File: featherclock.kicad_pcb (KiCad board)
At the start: 4 copper layers, 58.4 x 22.9 mm, 53 parts, among them J1 feather long, J2 feather short, J3 Conn_01x04, J4 USB_C_Receptacle_USB2.0, Q1 MMBT3904, Q2 MMBT3904, SW1 SW_Push, U1 ESP8285, U2 DS3231MZ, U3 74AHCT1G125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

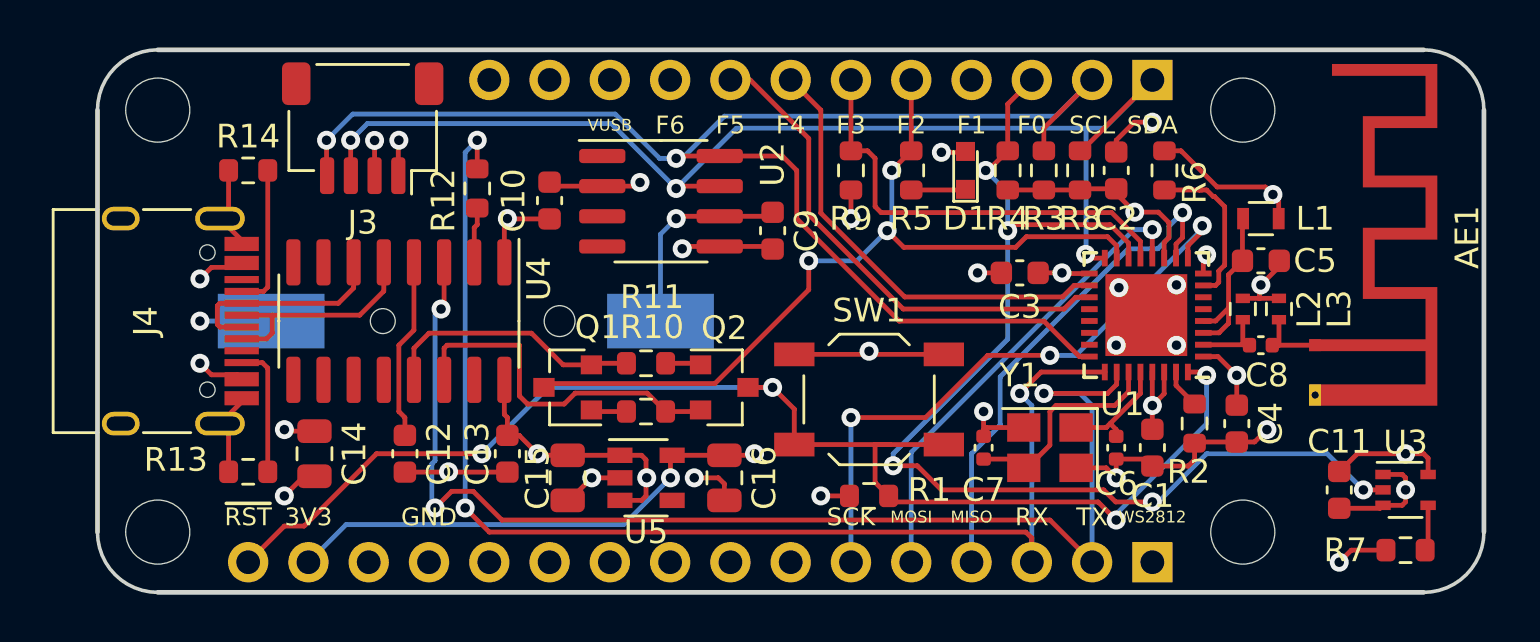
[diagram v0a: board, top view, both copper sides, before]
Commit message: Updated most 0603 packages to 0402
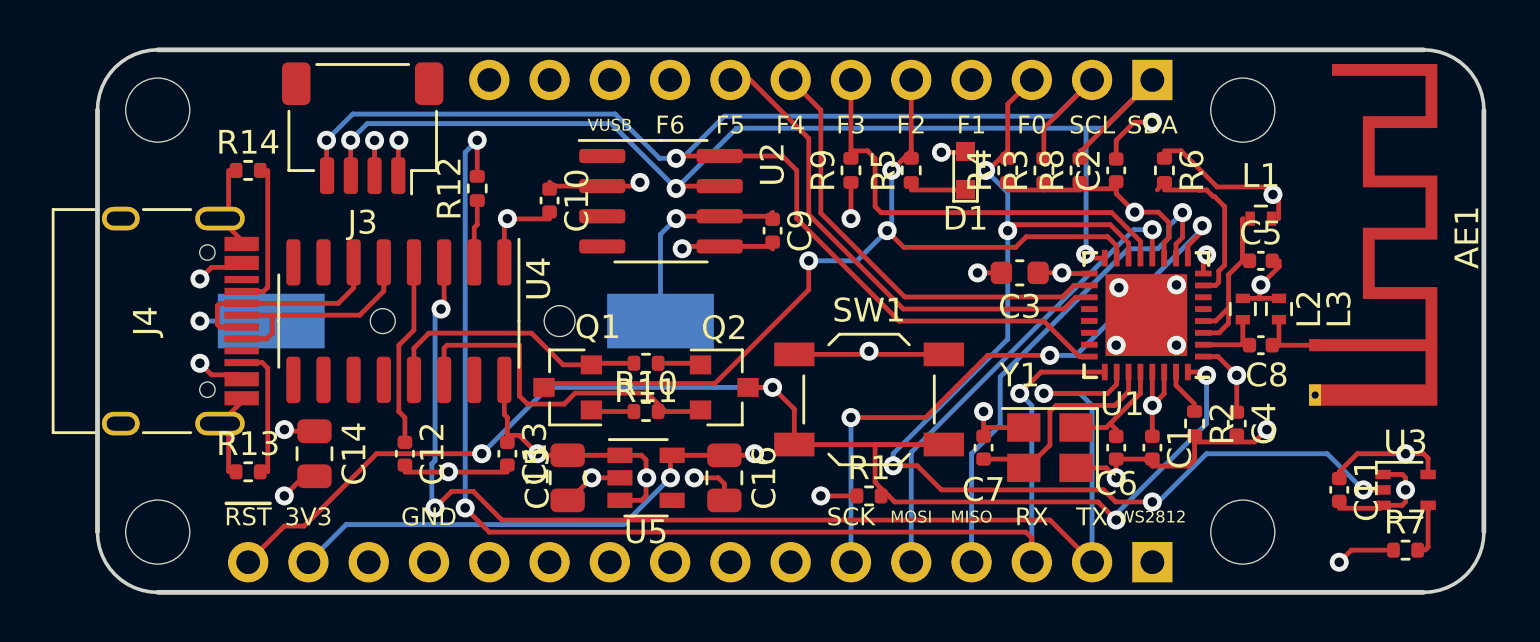
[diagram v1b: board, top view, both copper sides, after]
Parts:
- C1, C10, C11, C12, C13, C2, C4, C5, C9: footprint Capacitor_SMD:C_0603_1608Metric -> Capacitor_SMD:C_0402_1005Metric
- L1: footprint Inductors_SMD:L_0603 -> Inductors_SMD:L_0402
- R1, R10, R11, R12, R13, R14, R2, R3, R4, R5, R6, R7, R8, R9: footprint Resistor_SMD:R_0603_1608Metric -> Resistor_SMD:R_0402_1005Metric

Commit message: Cleaned up for new 0402 parts, and rearranged parts now that we have so much space.
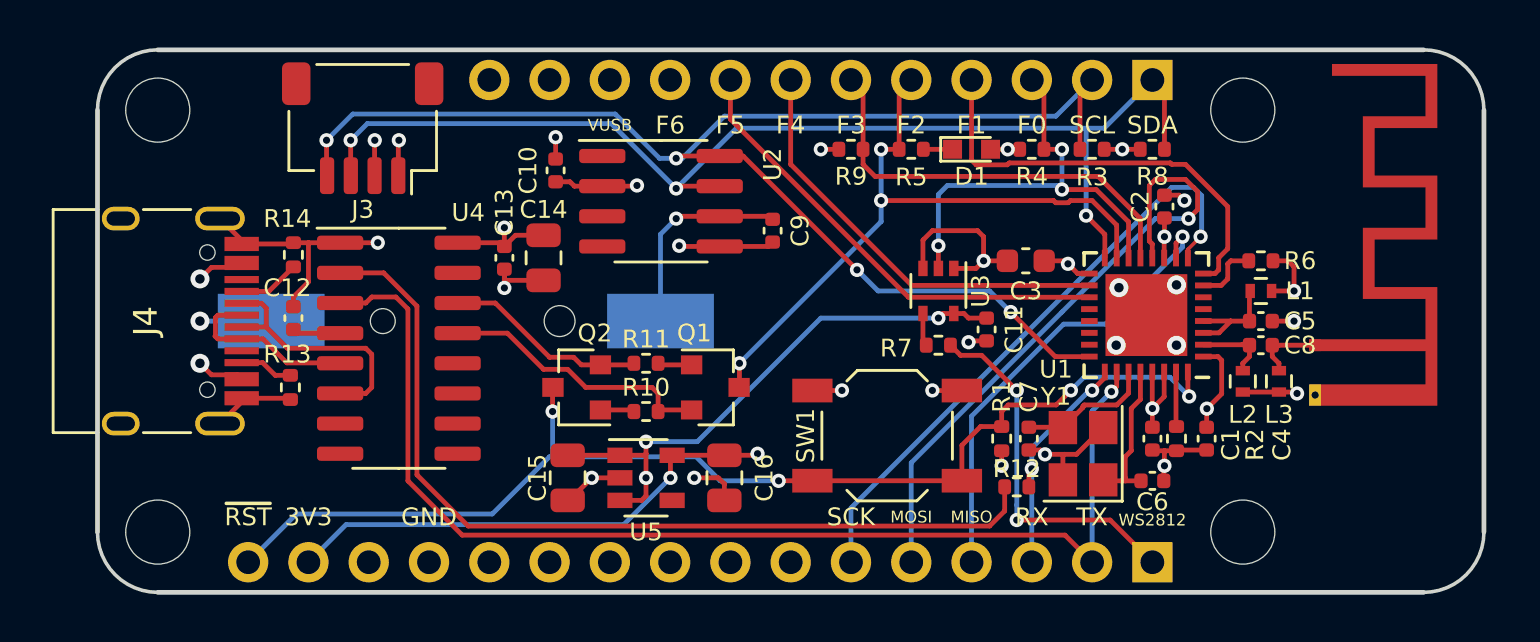
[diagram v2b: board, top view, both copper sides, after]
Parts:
- moved R12 26.0 mm to (64.1, 43.8), turned to 0 degrees
- moved R7 21.5 mm to (60.8, 37.8), turned to 180 degrees
- moved U3 21.4 mm to (60.8, 35.6), turned to 270 degrees
- moved C11 16.3 mm to (62.9, 37.2)
- moved C14 12.7 mm to (44.2, 34.2)
- moved C13 8.26 mm to (42.5, 34.2)
- moved C12 7.40 mm to (33.7, 36.7), turned to 90 degrees
- moved Q1 6.22 mm to (51.4, 39.6), turned to 0 degrees
- moved Q2 6.22 mm to (45.6, 39.6), turned to 180 degrees
- moved R1 6.09 mm to (63.5, 41.8), turned to 90 degrees
- moved R6 5.57 mm to (74.4, 34.3), turned to 180 degrees
- moved R14 4.03 mm to (33.7, 34.0), turned to 270 degrees
- moved R13 3.98 mm to (33.5, 39.6), turned to 90 degrees
- moved R8 3.17 mm to (69.8, 29.6), turned to 0 degrees
- moved L1 3.05 mm to (74.4, 35.6)
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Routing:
- net /RX: track 53.6 -> 10.2 mm, vias 3 -> 2
- net Net-(R12-Pad1): track 2.34 -> 37.9 mm
- net /GPIO2: track 48.4 -> 19.0 mm, vias 5 -> 3
- net VCC: track 21.6 -> 32.2 mm
- net +3V3: track 53.6 -> 44.6 mm, vias 11 -> 12
- net GND: track 64.7 -> 56.8 mm, vias 21 -> 22
- net /RESET: track 56.8 -> 49.3 mm
- net /GPIO0: track 35.5 -> 28.2 mm
- net /GPIO13-MOSI: track 19.9 -> 26.9 mm
- net /RTS: track 15.0 -> 8.54 mm
- net Net-(C12-Pad1): track 7.66 -> 2.03 mm
- net /WS2812: track 10.7 -> 15.5 mm, vias 1 -> 2
- net Net-(R6-Pad2): track 7.02 -> 2.72 mm
- net Net-(C7-Pad1): track 9.25 -> 5.73 mm
- net Net-(J4-PadA5): track 6.09 -> 2.61 mm
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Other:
- net class Default: clearance 0.2 -> 0.1524; trace_width 0.25 -> 0.1524; via_dia 0.8 -> 0.6; via_drill 0.4 -> 0.3
- rule trace_clearance: 0.2 -> 0.1524
- rule via_min_drill: 0.3 -> 0.2

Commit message: Added tooling holes and fiducials. Extended board outline under USB connector. Ran DRC, looks good - can probably order these now.
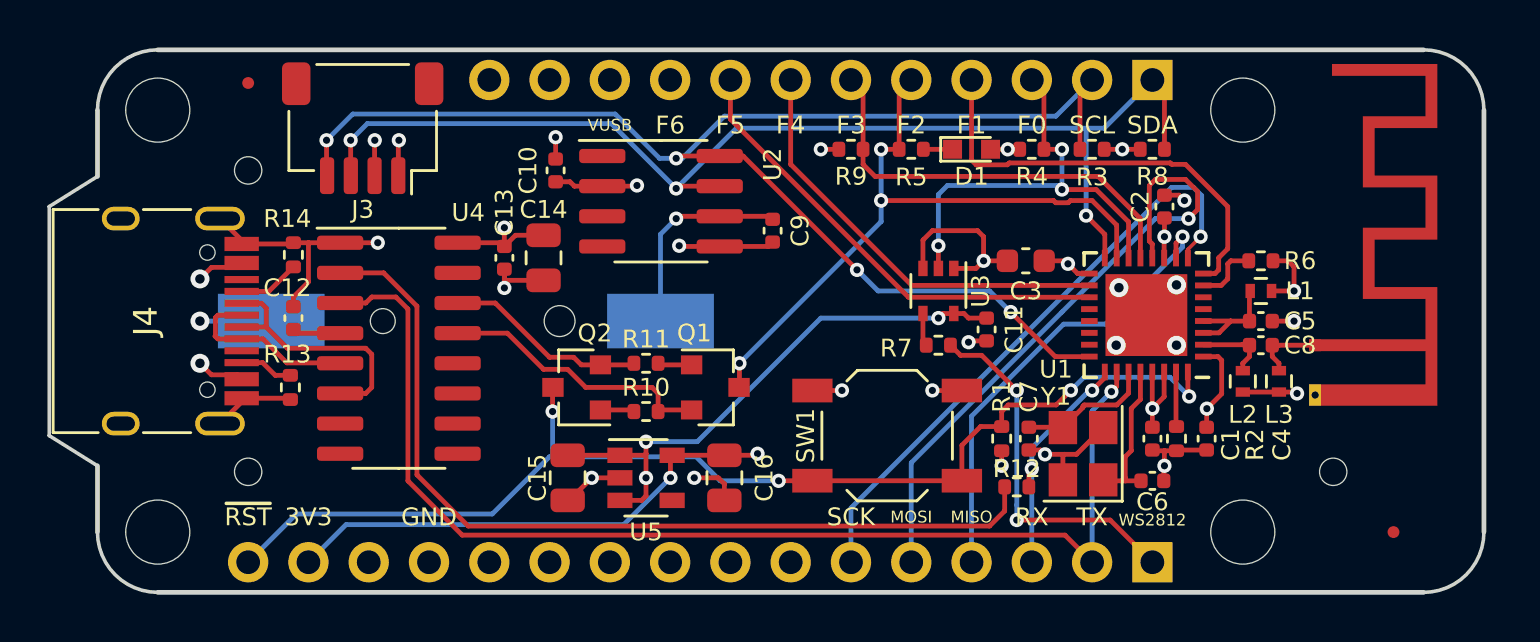
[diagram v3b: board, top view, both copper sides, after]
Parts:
- added REF**: Fiducial_0.5mm_Mask1.5mm, Fiducial:Fiducial_0.5mm_Mask1.5mm, F.Cu at (31.8, 26.8)
- added REF**: Fiducial_0.5mm_Mask1.5mm, Fiducial:Fiducial_0.5mm_Mask1.5mm, F.Cu at (80.0, 45.7)
- added REF**: tooling-hole, jlcpcb-tooling:tooling-hole, F.Cu at (31.8, 43.2)
- added REF**: tooling-hole, jlcpcb-tooling:tooling-hole, F.Cu at (31.8, 30.5)
- added REF**: tooling-hole, jlcpcb-tooling:tooling-hole, F.Cu at (77.5, 43.2)
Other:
- board size 58.4 x 22.9 mm -> 60.5 x 22.9 mm

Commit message: Adding ADC and enable pins
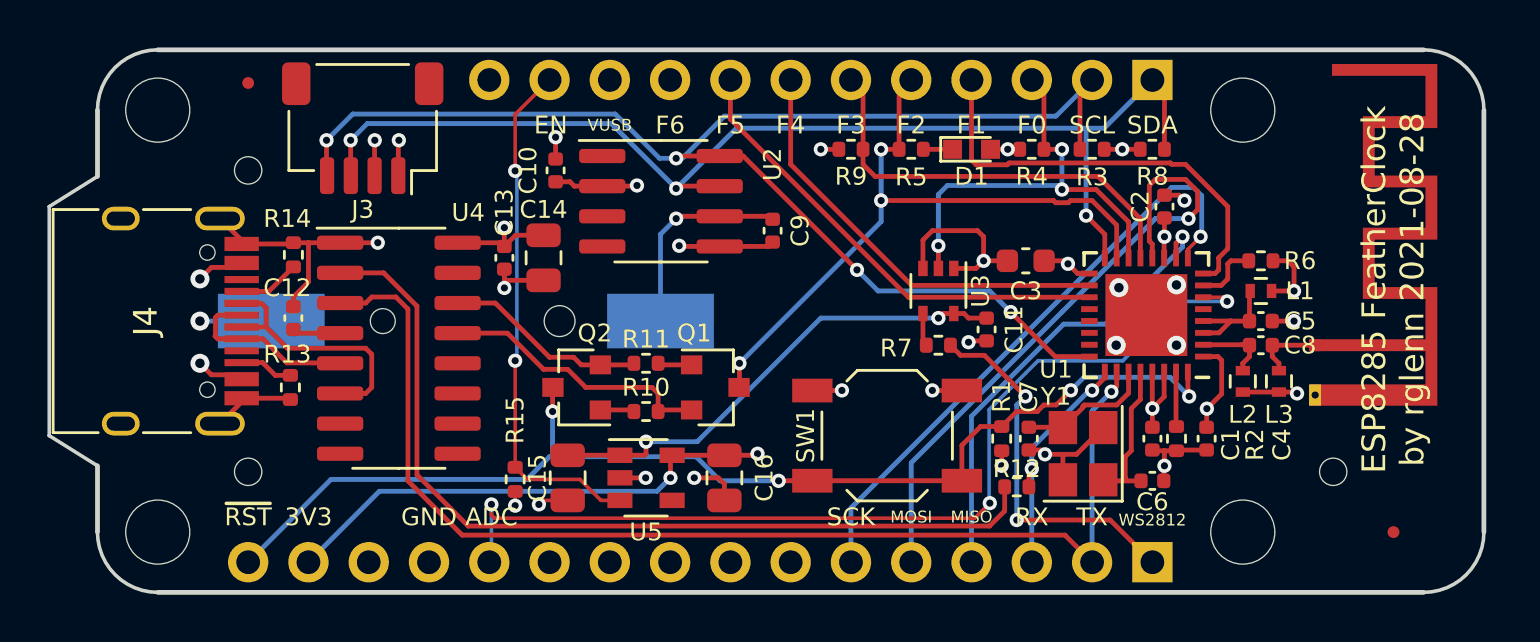
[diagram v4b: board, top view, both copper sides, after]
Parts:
- added R15: 10K, Resistor_SMD:R_0402_1005Metric, F.Cu at (43.0, 43.5)
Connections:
- J1 pad 12: Net-(J1-Pad12) -> /ADC
- U5 pad 3: VCC -> /EN
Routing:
- net /ADC: track 0.00 -> 41.5 mm, vias 0 -> 3
- net /EN: track 0.00 -> 22.0 mm, vias 0 -> 2
- net VCC: track 32.2 -> 29.8 mm
- net GND: track 56.8 -> 56.7 mm, vias 22 -> 23
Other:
- board text added: "ADC"
- board text added: "EN"
- board text added: "ESP8285 FeatherClock by rglenn 2021-08-28"
